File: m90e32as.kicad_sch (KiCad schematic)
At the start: 90 parts, among them J2 MX15EDGRHC-3.5-2x03P, J3 MX15EDGKNH-3.5-2x03P, U10 DB126V-5.0-2P-BK-P, U5 ATM90E32AS-AU-R, U6 K3-2268P, U7 TLP291-4, U8 TLP291-4, U9 DB126V-5.0-2P-BK-P, Y1 ABM8G-16.384MHZ-18-D2Y-T

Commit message: Add MX15EDGRHC-3.5-2x03P footprint and update M90E32AS connector
Adds the new project-local footprint and repoints the M90E32AS
6-pin connector to it, plus resulting PCB layout and project
metadata updates.

Co-Authored-By: Claude Sonnet 5 <noreply@anthropic.com>
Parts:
- J2: footprint ra5_2022:CONN-TH_6P-P3.50x2.50_MAX_MX15EDGRHC-3.5-2x03P -> ra5_2022:MX15EDGRHC-3.5-2x03P
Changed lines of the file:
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@@
 			)
 		)
-		(property "Footprint" "ra5_2022:CONN-TH_6P-P3.50x2.50_MAX_MX15EDGRHC-3.5-2x03P"
+		(property "Footprint" "ra5_2022:MX15EDGRHC-3.5-2x03P"
 			(at 96.52 187.96 0)
 			(hide yes)
@@
 			(hide yes)
 			(show_name no)
+			(do_not_autoplace no)
+			(effects
+				(font
+					(size 1.27 1.27)
+				)
+			)
+		)
+		(property "LCSC Part #" ""
+			(at 91.44 176.53 0)
+			(hide yes)
+			(show_name no)

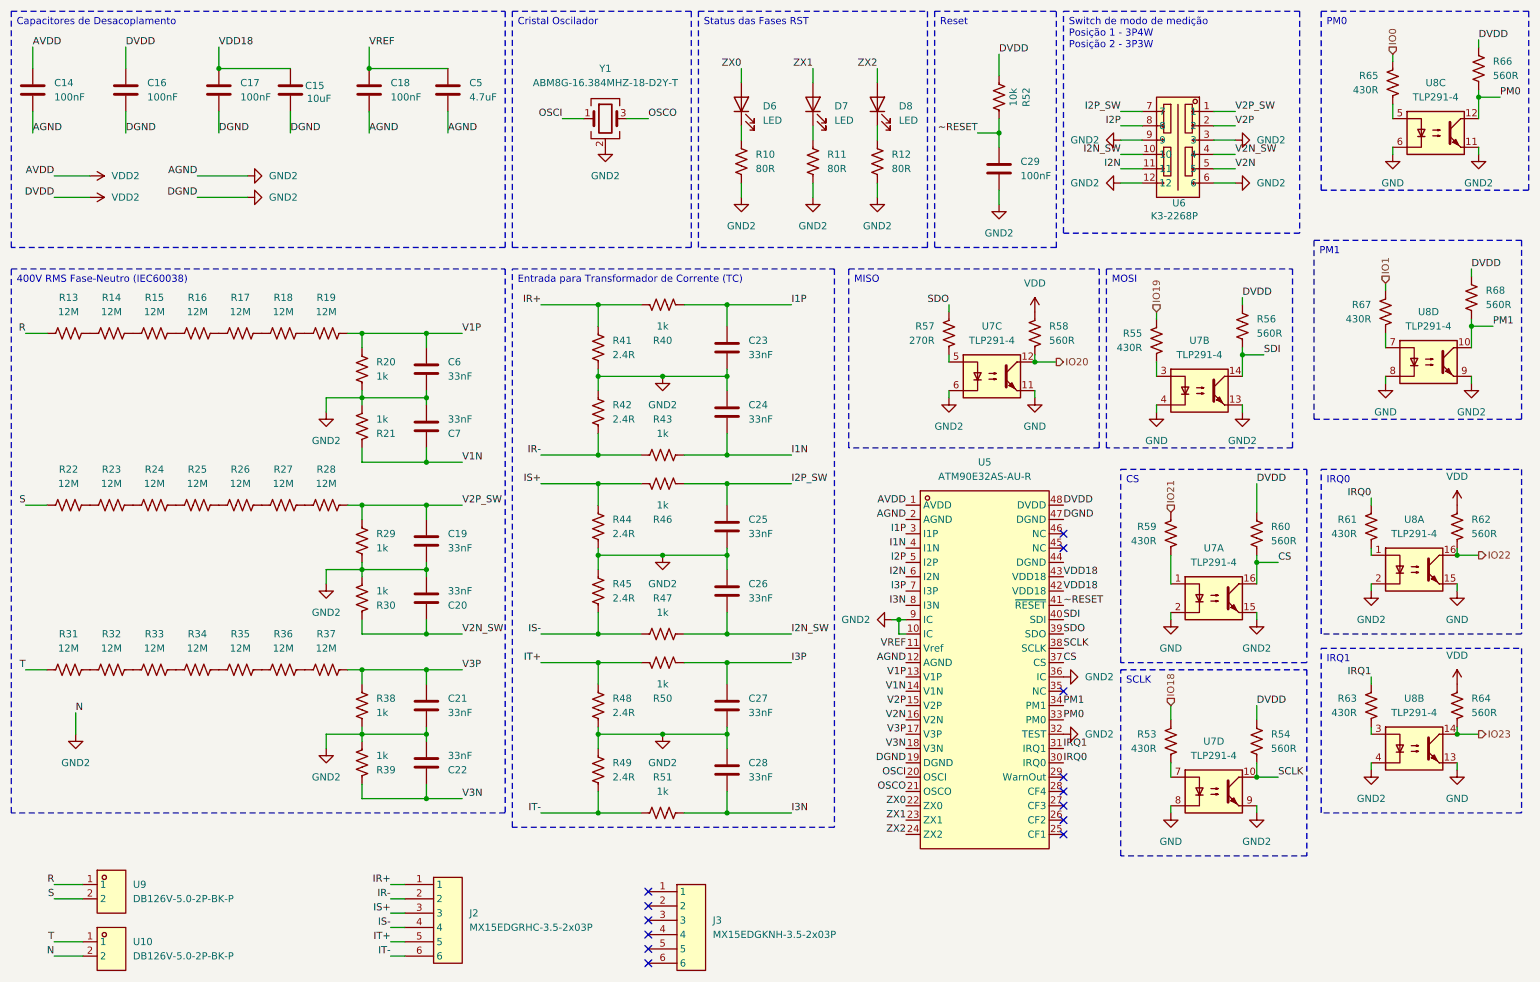
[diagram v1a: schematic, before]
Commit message: Checkpoint: MCU/M90E32AS/power_source rework, PCB layout, new sheets, library imports
- Rework mcu.kicad_sch, m90e32as.kicad_sch and power_source.kicad_sch: PM0/PM1/
  IRQ0/IRQ1 isolation wiring for the M90E32AS, USB-C native USB wiring, and
  related connector updates.
- Add analog_io.kicad_sch and digital_io.kicad_sch hierarchical sheets.
- Update ra5_2022.kicad_pcb layout and ra5_2022.kicad_pro settings.
- Import several LCSC components into the project library (connectors,
  inductor, SOT/SOIC footprints, USB-C connectors, power module).
- Fix import_lcsc_component.sh to normalize the "LCSC Part" field name to
  "LCSC Part #" on imported footprints too (previously only on symbols).
- Ignore local .claude/ state (worktrees/session data) in .gitignore.

Co-Authored-By: Claude Sonnet 5 <noreply@anthropic.com>
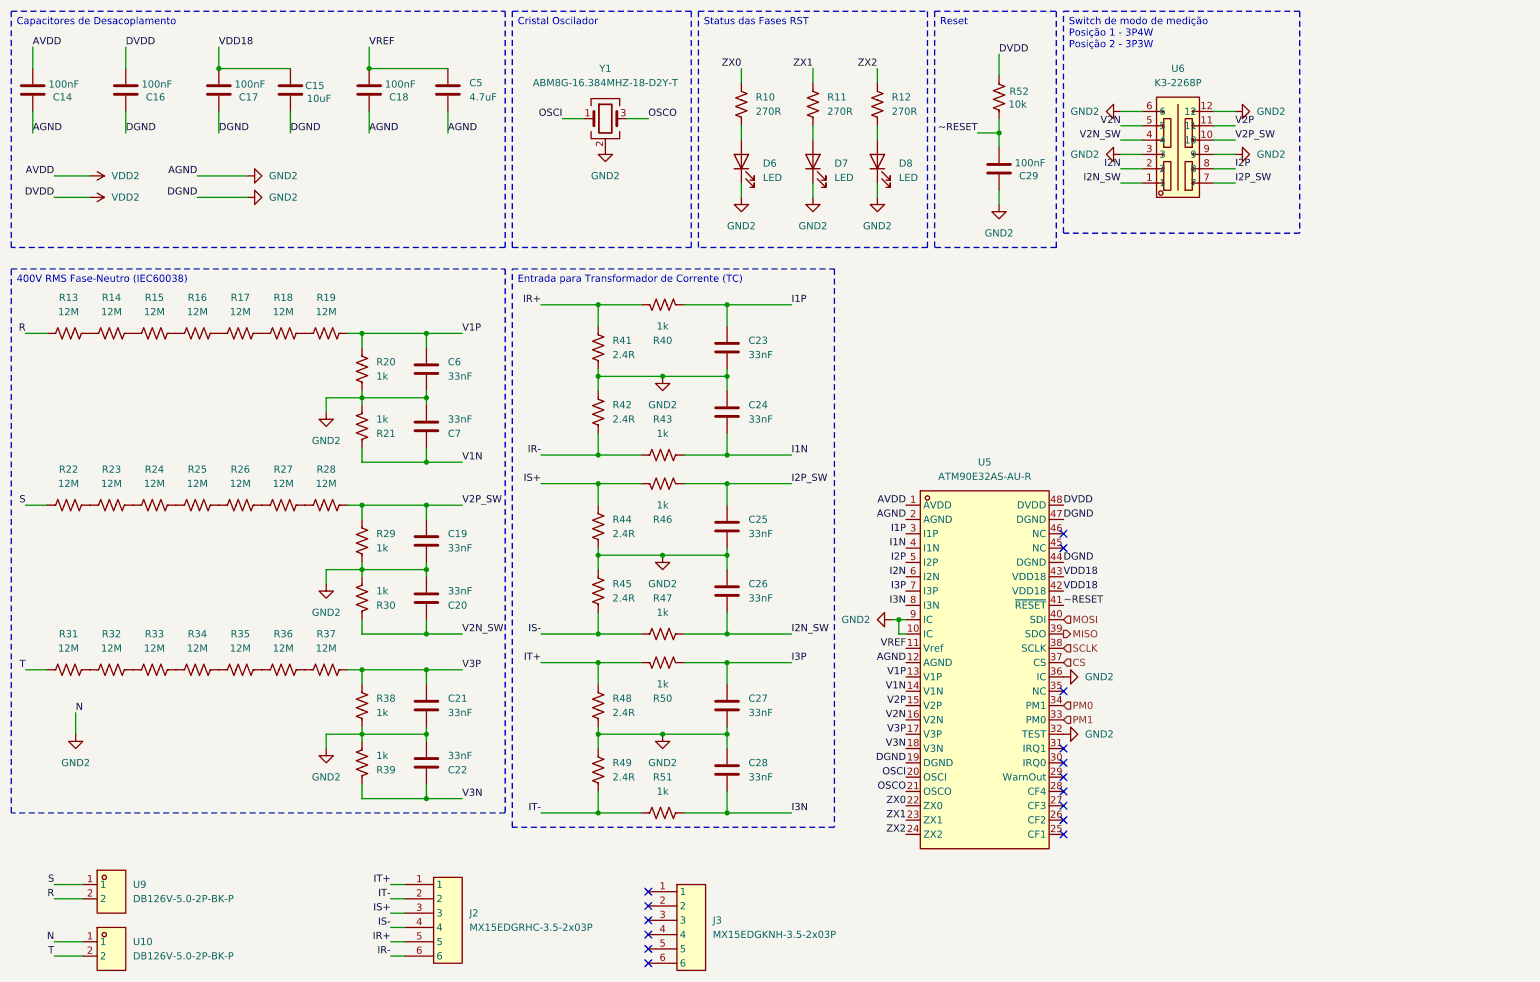
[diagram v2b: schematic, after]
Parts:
- removed R53, R55, R59, R61, R63, R65, R67: 430R, Resistor_SMD:R_0402_1005Metric, symbol Device:R_US
- removed R54, R56, R58, R60, R62, R64, R66, R68: 560R, Resistor_SMD:R_0402_1005Metric, symbol Device:R_US
- removed R57: 270R, Resistor_SMD:R_0402_1005Metric, symbol Device:R_US
- removed U7, U8: TLP291-4, Package_SO:SOIC-16_4.55x10.3mm_P1.27mm, symbol Isolator:TLP291-4
- C14, C16, C17, C18, C29: footprint Capacitor_SMD:C_0402_1005Metric -> Capacitor_SMD:C_0201_0603Metric; LCSC Part # C22435941 -> C7393837; MPN CGA0402X7R104J250GT -> TCC0201X7R104K100ZT
- J2: LCSC Part C49142489 -> (none); LCSC Part # (none) -> C49142489
- J3: LCSC Part C49142469 -> (none); LCSC Part # (none) -> C49142469
- R10, R11, R12: value 80R -> 270R; footprint Resistor_SMD:R_0603_1608Metric -> Resistor_SMD:R_0402_1005Metric; LCSC Part # C2077036 -> C54920764; MPN CRCW060382R0FKEAC -> HRC0402J271 DNTO
- R13, R14, R15, R16, R17, R18, R19, R22, R23, R24, R25, R26, R27, R28, R31, R32, R33, R34, R35, R36, R37: LCSC Part # 1206 -> C5126174
- U10, U9: LCSC Part C49260677 -> (none); LCSC Part # (none) -> C49260677
- U5: LCSC Part C177153 -> (none); LCSC Part # (none) -> C177153
- U6: LCSC Part C502352 -> (none); LCSC Part # (none) -> C502352
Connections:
- net GND2: now also C14.1, C16.1, C17.1, C18.1, C29.1, D6.1 (K), D7.1 (K), D8.1 (K), U10.1, U5.44 (DGND); no longer C14.2, C16.2, C17.2, C18.2, C29.2, R10.2, R11.2, R12.2, U10.2
- net I2N: now also U6.2; no longer U6.11
- net I2N_SW: now also U6.1; no longer U6.10
- net IR+: now also J2.5; no longer J2.1
- net IR-: now also J2.6; no longer J2.2
- net IT+: now also J2.1; no longer J2.5
- net IT-: now also J2.2; no longer J2.6
- net PM0: now also U5.34 (PM1); no longer U5.33 (PM0)
- net PM1: now also U5.33 (PM0); no longer U5.34 (PM1)
- net R: now also U9.2; no longer U9.1
- net S: now also U9.1; no longer U9.2
- net T: now also U10.2; no longer U10.1
- net V2P: now also U6.11; no longer U6.2
- net V2P_SW: now also U6.10; no longer U6.1
- net VDD18: now also C17.2; no longer C17.1
- net VDD2: now also C14.2, C16.2; no longer C14.1, C16.1
- net VREF: now also C18.2; no longer C18.1
- net ZX0: now also R10.1; no longer D6.2 (A)
- net ZX1: now also R11.1; no longer D7.2 (A)
- net ZX2: now also R12.1; no longer D8.2 (A)
- net ~RESET: now also C29.2; no longer C29.1
- net IRQ0: no longer names the net of U5.30 (IRQ0)
- net IRQ1: no longer names the net of U5.31 (IRQ1)
- net SDI renamed MOSI
- net SDO renamed MISO
- new net: D7.2 (A), R11.2
- new net: D6.2 (A), R10.2
- new net: D8.2 (A), R12.2
- no-connect marks 14 -> 16
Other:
- moved on the sheet: D6, D7, D8, R10

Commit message: Checkpoint: RA5 base board finished, M.2 shield interconnect defined
Base board (ra5_2022):
- Finalize component placement on ra5_2022.kicad_pcb; next step is routing
- Add STM8S003F3P to bridge the 2 digital inputs / 2 digital outputs onto
  the shared I2C bus (alongside the ADS1115), freeing up M.2 pins
- Wire J1 (M.2 Key-E) to a custom, non-spec-compliant 3.3V pinout: I2C
  (SDA/SCL/ALERT#) on the native pins, M90E32AS SPI reusing the SD/SDIO
  "SPI mode" pin convention (SCLK/MOSI/MISO/CS), PM0/PM1 on VENDOR_DEFINED
  pins, USB-C passthrough, full GND/VDD
- Fix AS0BC21-S40BE-7H footprint: pads 76/77 (shield/ground tabs, not part
  of the 75-pin M.2 spec) remapped onto the GND pin instead of dangling
- Swap the buck inductor (L2) for SLW5040S100MST (C182189): same 10uH,
  lower DCR, 5x5mm footprint to clear a routing constraint
- Remove the unused "Production" KiCad Design Variant and align the
  remaining "Develop" variant's footprints with the defaults -- a
  variant/default footprint mismatch was causing Update PCB from Schematic
  to silently duplicate footprints on every sync
- Clean up 10 further orphaned duplicate footprints left on the PCB from
  earlier design revisions (R11, R12, C14, C16, C17, C18, C29, C31, C32, C35)
- Fix 3D model paths across the shared library to use the RA5_2022_LIB
  environment variable instead of ${KIPRJMOD}, so previews resolve
  correctly from sibling projects too

New sibling project (ra5_shield_modem/):
- MCU + LTE modem card, built to the M.2 Key-E mechanical form factor to
  plug into the base board's J1
- Share the ra5_2022 parts library via sym-lib-table/fp-lib-table
- Add the timonsku/M.2-Card-Footprints submodule as a card-edge template

Co-Authored-By: Claude Sonnet 5 <noreply@anthropic.com>
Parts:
- renumbered C14 to C19, C16 to C20, C17 to C21, C15 to C22, C18 to C23, C6 to C24, C7 to C25, C19 to C26, C20 to C27, C21 to C28, C22 to C29, C5 to C30, C23 to C31, C24 to C32, C25 to C33, C26 to C34, C27 to C35, C28 to C36, C29 to C37, D6 to D4, D7 to D5, D8 to D6, J2 to J3, J3 to J4, R13 to R12, R22 to R13, R31 to R14, R14 to R15, R23 to R16, R32 to R17, R15 to R18, R24 to R19, R33 to R20, R16 to R21, R25 to R22, R34 to R23, R17 to R24, R26 to R25, R35 to R26, R18 to R27, R27 to R28, R36 to R29, R19 to R30, R28 to R31, R37 to R32, R20 to R33, R21 to R34, R29 to R35, R30 to R36, R38 to R37, R39 to R38, R41 to R39, R42 to R40, R44 to R41, R45 to R42, R48 to R43, R49 to R44, R40 to R45, R43 to R46, R46 to R47, R47 to R48, R50 to R49, R51 to R50, R10 to R51, R11 to R52, R12 to R53, R52 to R54, U5 to U10, U6 to U11, U9 to U8, U10 to U9
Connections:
- net GND2: now also C25.1, C27.1, C29.1, R34.1, R36.1, R38.1; no longer C25.2, C27.2, C29.2, R34.2, R36.2, R38.2
- net V1N: now also C25.2, R34.2; no longer C25.1, R34.1
- net V2N_SW: now also C27.2, R36.2; no longer C27.1, R36.1
- net V3N: now also C29.2, R38.2; no longer C29.1, R38.1
